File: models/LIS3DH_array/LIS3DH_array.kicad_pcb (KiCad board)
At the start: 2 copper layers, 113 x 113 mm, 130 parts, among them U1 LIS3DH, U10 LIS3DH, U11 LIS3DH, U12 LIS3DH, U13 LIS3DH, U14 LIS3DH, U15 LIS3DH, U16 LIS3DH, U2 LIS3DH, U3 LIS3DH, U4 LIS3DH, U5 LIS3DH, U6 LIS3DH, U7 LIS3DH, U8 LIS3DH, U9 LIS3DH

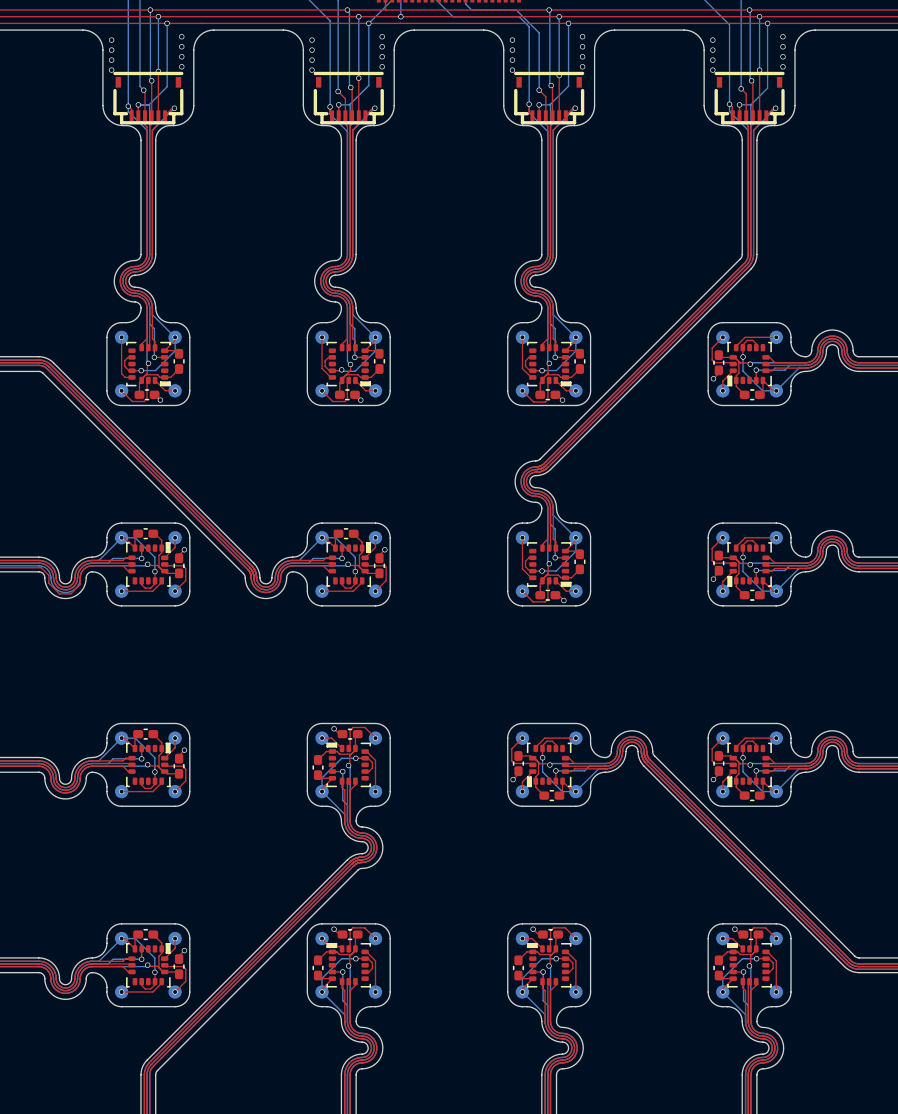
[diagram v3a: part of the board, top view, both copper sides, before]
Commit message: added or gate on each acc to prevent I2C interference when the chip have CSB high
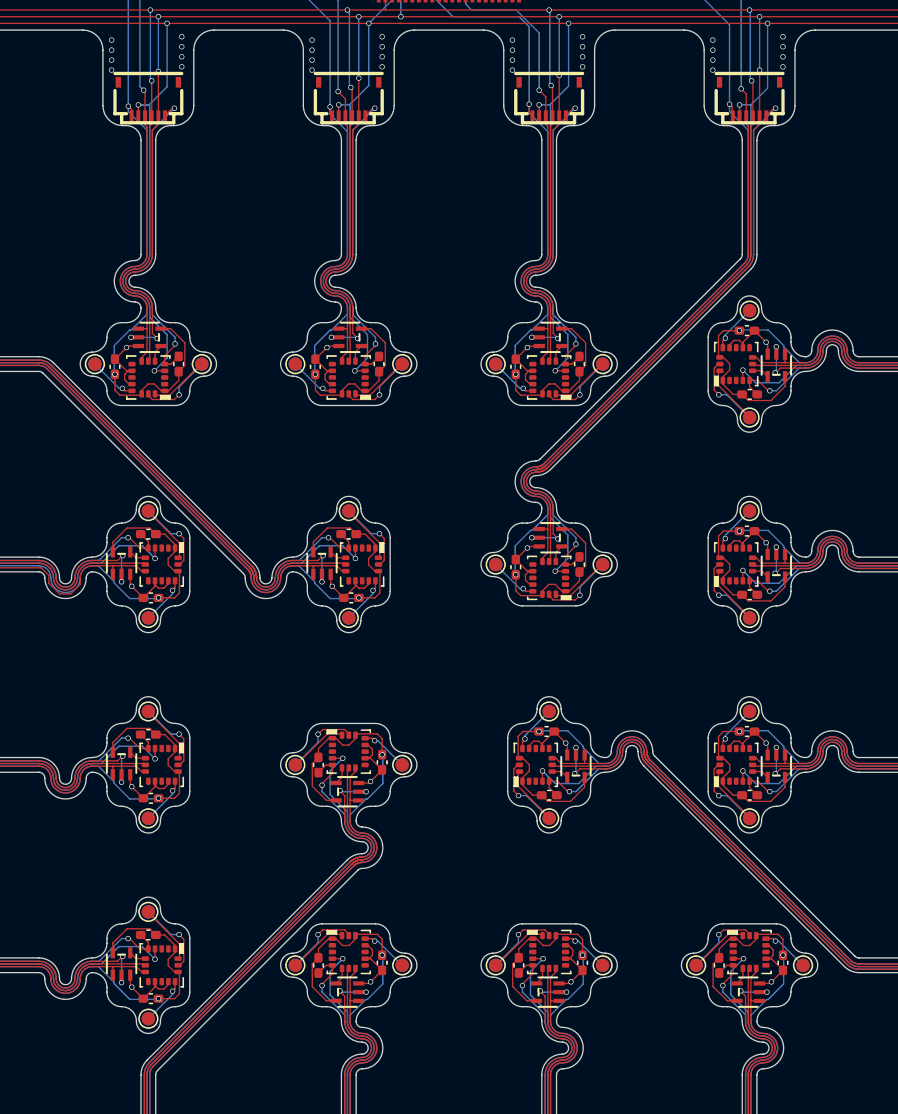
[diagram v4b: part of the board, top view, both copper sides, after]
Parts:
- added U17: SN74LVC1G32DCKR, 00_lcsc:SOT-353_L2.1-W1.3-P0.65-LS2.3-BR, F.Cu at (100.1, 78.0)
- added U18: SN74LVC1G32DCKR, 00_lcsc:SOT-353_L2.1-W1.3-P0.65-LS2.3-BR, F.Cu at (115.1, 78.0)
- added U19: SN74LVC1G32DCKR, 00_lcsc:SOT-353_L2.1-W1.3-P0.65-LS2.3-BR, F.Cu at (130.1, 78.0)
- added U20: SN74LVC1G32DCKR, 00_lcsc:SOT-353_L2.1-W1.3-P0.65-LS2.3-BR, F.Cu at (147.0, 80.1)
- added U21: SN74LVC1G32DCKR, 00_lcsc:SOT-353_L2.1-W1.3-P0.65-LS2.3-BR, F.Cu at (98.0, 94.9)
- added U22: SN74LVC1G32DCKR, 00_lcsc:SOT-353_L2.1-W1.3-P0.65-LS2.3-BR, F.Cu at (113.0, 94.9)
- added U23: SN74LVC1G32DCKR, 00_lcsc:SOT-353_L2.1-W1.3-P0.65-LS2.3-BR, F.Cu at (130.1, 93.0)
- added U24: SN74LVC1G32DCKR, 00_lcsc:SOT-353_L2.1-W1.3-P0.65-LS2.3-BR, F.Cu at (147.0, 95.1)
- added U25: SN74LVC1G32DCKR, 00_lcsc:SOT-353_L2.1-W1.3-P0.65-LS2.3-BR, F.Cu at (98.0, 109.9)
- added U26: SN74LVC1G32DCKR, 00_lcsc:SOT-353_L2.1-W1.3-P0.65-LS2.3-BR, F.Cu at (114.9, 112.0)
- added U27: SN74LVC1G32DCKR, 00_lcsc:SOT-353_L2.1-W1.3-P0.65-LS2.3-BR, F.Cu at (132.0, 110.1)
- added U28: SN74LVC1G32DCKR, 00_lcsc:SOT-353_L2.1-W1.3-P0.65-LS2.3-BR, F.Cu at (147.0, 110.1)
- added U29: SN74LVC1G32DCKR, 00_lcsc:SOT-353_L2.1-W1.3-P0.65-LS2.3-BR, F.Cu at (98.0, 124.9)
- added U30: SN74LVC1G32DCKR, 00_lcsc:SOT-353_L2.1-W1.3-P0.65-LS2.3-BR, F.Cu at (114.9, 127.0)
- added U31: SN74LVC1G32DCKR, 00_lcsc:SOT-353_L2.1-W1.3-P0.65-LS2.3-BR, F.Cu at (129.9, 127.0)
- added U32: SN74LVC1G32DCKR, 00_lcsc:SOT-353_L2.1-W1.3-P0.65-LS2.3-BR, F.Cu at (144.9, 127.0)
- TP1, TP2, TP28, TP29, TP3, TP30, TP31, TP32, TP33, TP34, TP35, TP36, TP37, TP4, TP40, TP41, TP44, TP45, TP48, TP49, TP5, TP52, TP53, TP56, TP57, TP6, TP60, TP61, TP64, TP7, TP8, TP9: moved to F.Cu
- moved TP28 6.33 mm to (96.0, 80.0)
- moved TP29 6.33 mm to (111.0, 80.0)
- moved TP30 6.33 mm to (126.0, 80.0)
- moved TP34 6.33 mm to (126.0, 95.0)
- moved TP58 6.33 mm to (126.0, 125.0)
- moved TP62 6.33 mm to (141.0, 125.0)
- moved TP38 6.33 mm to (111.0, 110.0)
- moved TP54 6.33 mm to (111.0, 125.0)
- moved TP31 6.32 mm to (145.0, 76.0)
- moved TP32 6.32 mm to (100.0, 99.0)
- moved TP33 6.32 mm to (115.0, 99.0)
- moved TP35 6.32 mm to (145.0, 91.0)
- moved TP36 6.32 mm to (100.0, 114.0)
- moved TP44 6.32 mm to (130.0, 106.0)
- moved TP48 6.32 mm to (145.0, 106.0)
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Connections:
- U1 pad 6: SDI -> Net-(U1-SDA/SDI/SDO)
- U10 pad 6: SDI -> Net-(U10-SDA/SDI/SDO)
- U11 pad 6: SDI -> Net-(U11-SDA/SDI/SDO)
- U12 pad 6: SDI -> Net-(U12-SDA/SDI/SDO)
- U13 pad 6: SDI -> Net-(U13-SDA/SDI/SDO)
- U14 pad 6: SDI -> Net-(U14-SDA/SDI/SDO)
- U15 pad 6: SDI -> Net-(U15-SDA/SDI/SDO)
- U16 pad 6: SDI -> Net-(U16-SDA/SDI/SDO)
- U2 pad 6: SDI -> Net-(U18-Y)
- U3 pad 6: SDI -> Net-(U19-Y)
- U4 pad 6: SDI -> Net-(U20-Y)
- U5 pad 6: SDI -> Net-(U21-Y)
- U6 pad 6: SDI -> Net-(U22-Y)
- U7 pad 6: SDI -> Net-(U23-Y)
- U8 pad 6: SDI -> Net-(U24-Y)
- U9 pad 6: SDI -> Net-(U25-Y)
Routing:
- net VDD: track 1135.9 -> 1267.0 mm
- net SDI: track 895.9 -> 926.9 mm, vias 32 -> 64
- net Sclk: track 960.9 -> 989.5 mm
- net SDO: track 901.4 -> 917.4 mm
- net GND: track 595.6 -> 585.0 mm, vias 195 -> 179
- net /LIS3DH_unit5/ADC1: track 1.82 -> 4.50 mm, vias 1 -> 0
- net /LIS3DH_unit13/ADC1: track 1.82 -> 4.50 mm, vias 1 -> 0
- net /LIS3DH_unit9/ADC1: track 1.82 -> 4.50 mm, vias 1 -> 0
- net /LIS3DH_unit6/ADC1: track 1.82 -> 4.50 mm, vias 1 -> 0
- net /LIS3DH_unit11/ADC1: track 1.82 -> 4.50 mm, vias 1 -> 0
- net /LIS3DH_unit2/ADC1: track 1.82 -> 4.50 mm, vias 1 -> 0
- net /LIS3DH_unit1/ADC1: track 1.82 -> 4.50 mm, vias 1 -> 0
- net /LIS3DH_unit7/ADC1: track 1.82 -> 4.50 mm, vias 1 -> 0
- net /LIS3DH_unit3/ADC1: track 1.82 -> 4.50 mm, vias 1 -> 0
- net /LIS3DH_unit8/ADC1: track 1.82 -> 4.50 mm, vias 1 -> 0
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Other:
- outline, holes or cut-outs redrawn

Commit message: update
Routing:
- net GND: track 585.0 -> 603.4 mm, vias 179 -> 195
- net VDD: track 1267.0 -> 1278.1 mm
- net SDI: track 926.9 -> 930.0 mm
- net nCS_13: track 157.4 -> 159.2 mm
- net nCS_16: track 206.1 -> 207.8 mm
- net nCS_15: track 218.7 -> 220.5 mm
- net nCS_5: track 131.9 -> 133.6 mm
- net nCS_10: track 231.2 -> 233.0 mm
- net nCS_7: track 71.2 -> 73.0 mm
- net nCS_3: track 38.3 -> 40.1 mm
- net nCS_1: track 55.4 -> 57.2 mm
- net nCS_6: track 140.3 -> 142.0 mm
- net nCS_4: track 114.9 -> 116.7 mm
- net nCS_2: track 42.9 -> 44.7 mm
- net nCS_12: track 140.8 -> 142.5 mm
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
